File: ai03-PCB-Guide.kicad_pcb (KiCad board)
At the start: 2 copper layers, 24 parts, among them SW1 SW_Push, U1 ATmega32U4-AU, Y1 16MHz

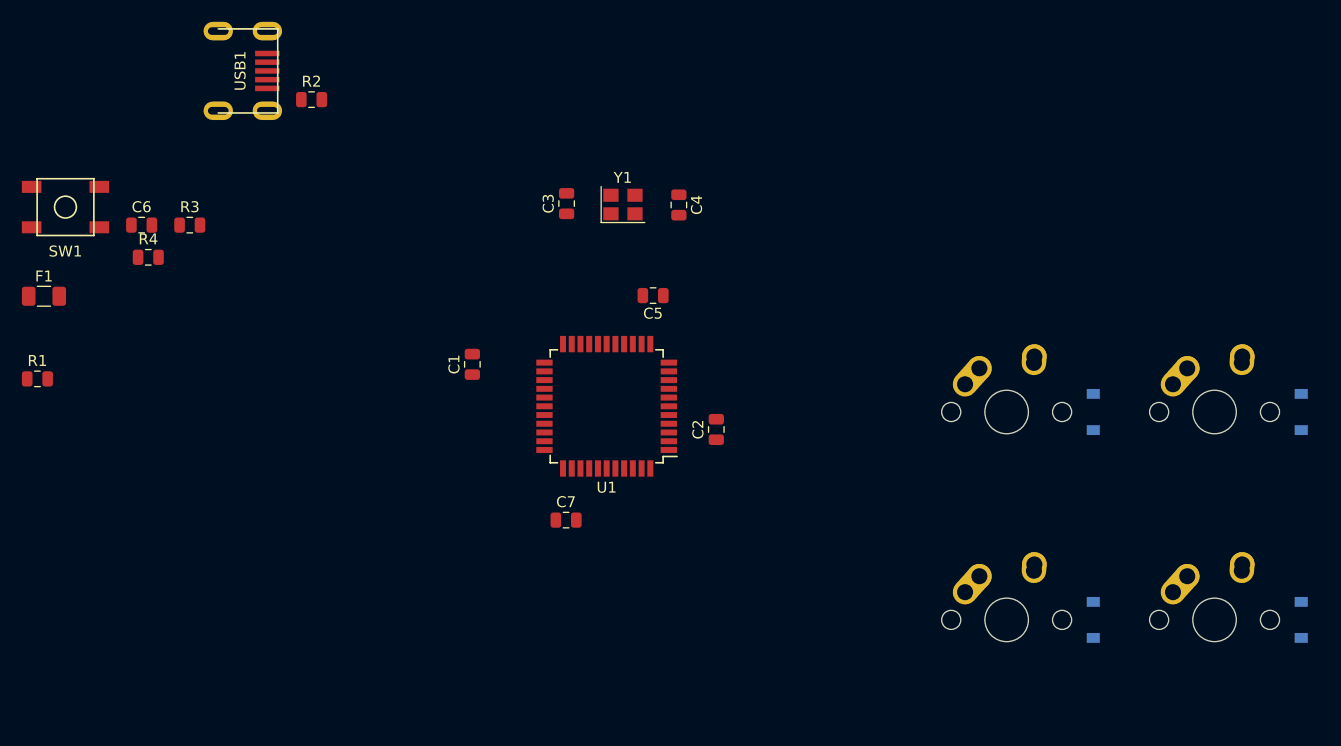
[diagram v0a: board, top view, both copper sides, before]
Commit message: Beginning Routing
This is the step just before the beginning of Routing. I've smoothed out the corners so as not to get cuts if it's printed. Setting a new Routing size called POWER for any power cables, and increasing the default size to 10mm. Now we connect everything together.
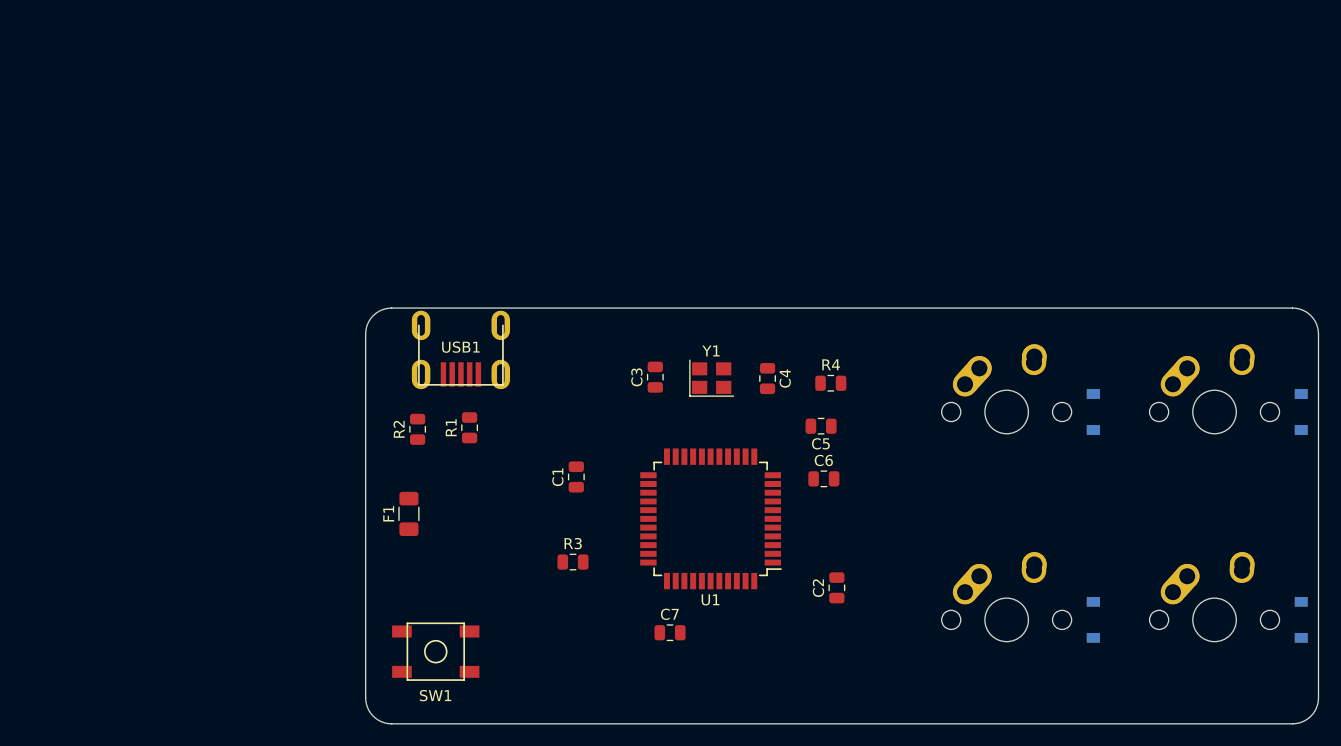
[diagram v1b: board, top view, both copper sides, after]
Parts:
- moved C6 66.7 mm to (153.1, 76.0)
- moved R4 63.6 mm to (153.7, 67.2)
- moved SW1 53.0 mm to (117.5, 91.8)
- moved R3 46.8 mm to (130.1, 83.6)
- moved R1 39.9 mm to (120.7, 71.3), turned to 90 degrees
- moved F1 38.9 mm to (115.1, 79.2), turned to 90 degrees
- moved USB1 32.2 mm to (119.9, 61.9), turned to 270 degrees
- moved R2 31.7 mm to (115.9, 71.4), turned to 90 degrees
- moved C5 19.5 mm to (152.9, 71.2)
- moved C2 18.2 mm to (154.3, 86.0)
- moved C4 17.9 mm to (148.0, 66.8)
- moved C3 17.9 mm to (137.7, 66.7)
- moved Y1 17.9 mm to (142.8, 66.7)
- moved U1 14.0 mm to (142.7, 79.6)
- moved C1 14.0 mm to (130.4, 75.8)
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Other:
- board outline added: 87.3 x 38.1 mm
- net class Default: trace_width 0.25 -> 0.254
- net class Power added: clearance 0.2, trace_width 0.381, via_dia 0.8, via_drill 0.4

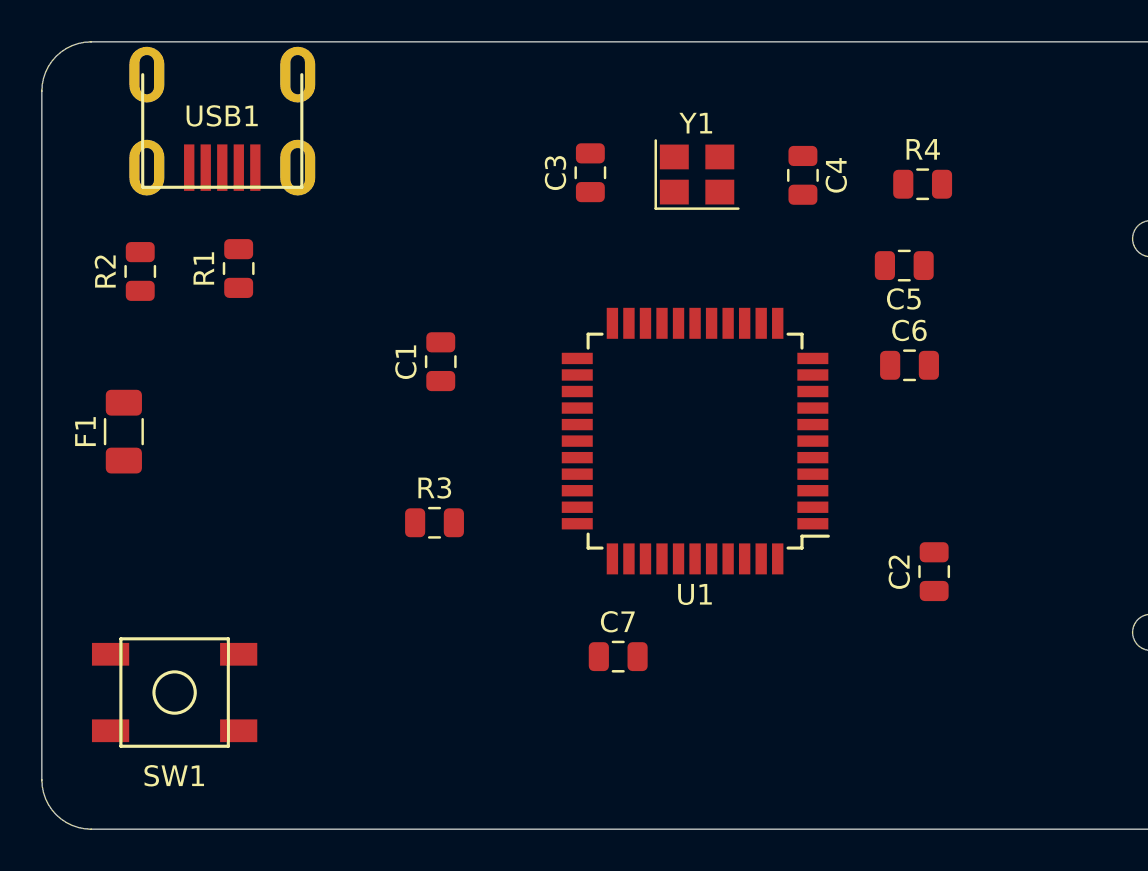
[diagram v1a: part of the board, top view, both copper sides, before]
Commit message: The bottom of the board
Hadn't put all the SMD components on the underside of the board. This is infuriating as it meant I basically had to flip and completely reorganise the layout of the SMD components.
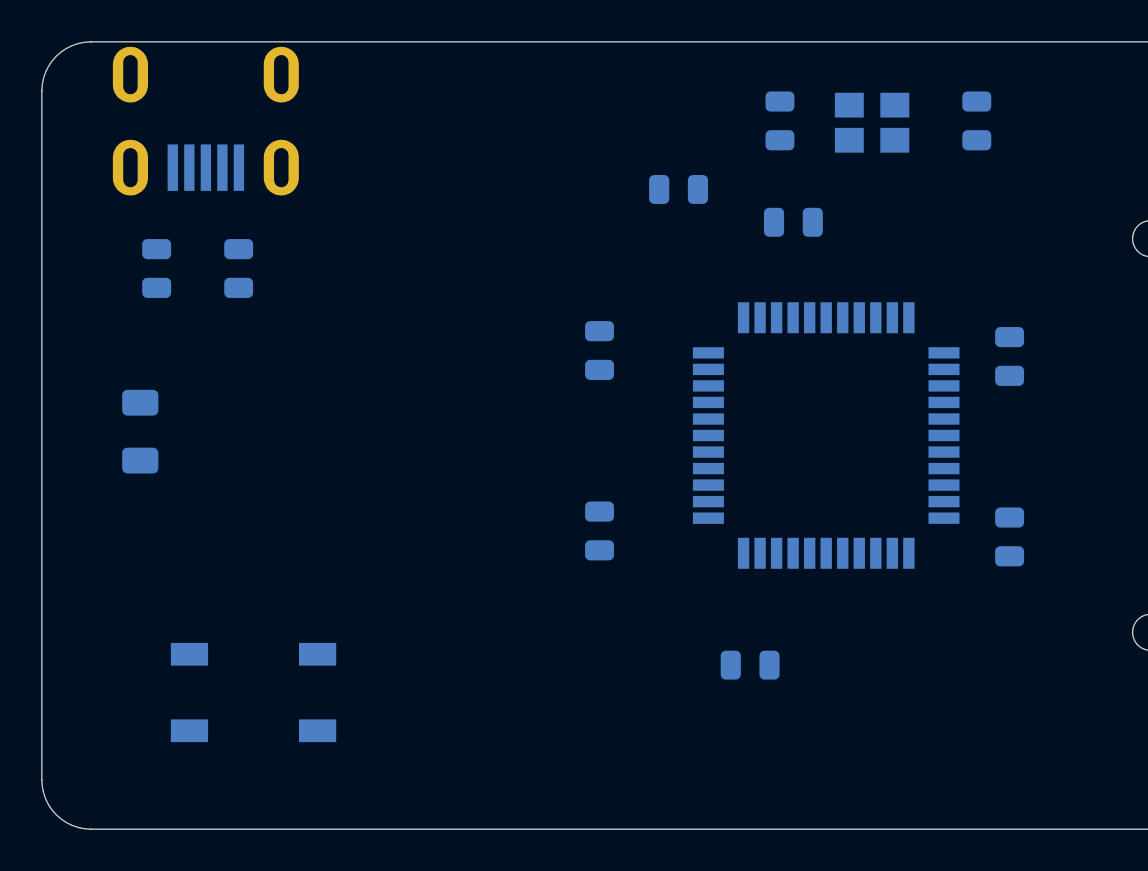
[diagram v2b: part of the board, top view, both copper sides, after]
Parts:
- C1, C2, C3, C4, C5, C6, C7, F1, R1, R2, R3, R4, SW1, U1, USB1, Y1: moved to B.Cu
- moved R3 27.8 mm to (158.0, 84.3), turned to 90 degrees
- moved C3 18.9 mm to (156.4, 64.2)
- moved C2 16.3 mm to (138.1, 84.0)
- moved C6 15.0 mm to (138.1, 75.3), turned to 270 degrees
- moved C1 14.2 mm to (141.9, 67.5), turned to 0 degrees
- moved Y1 8.83 mm to (151.3, 64.2), turned to 180 degrees
- moved C5 6.73 mm to (158.0, 75.5), turned to 90 degrees
- moved R4 6.52 mm to (147.5, 69.1), turned to 180 degrees
- moved C7 6.40 mm to (145.4, 90.5)
- moved U1 6.35 mm to (149.1, 79.4), turned to 0 degrees
- moved R2 4.76 mm to (120.7, 71.3)
- moved R1 3.97 mm to (116.7, 71.3)
- moved SW1 3.82 mm to (121.4, 91.8), turned to 180 degrees
- moved C4 2.86 mm to (146.8, 64.2)
- moved F1 0.79 mm to (115.9, 79.2)
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
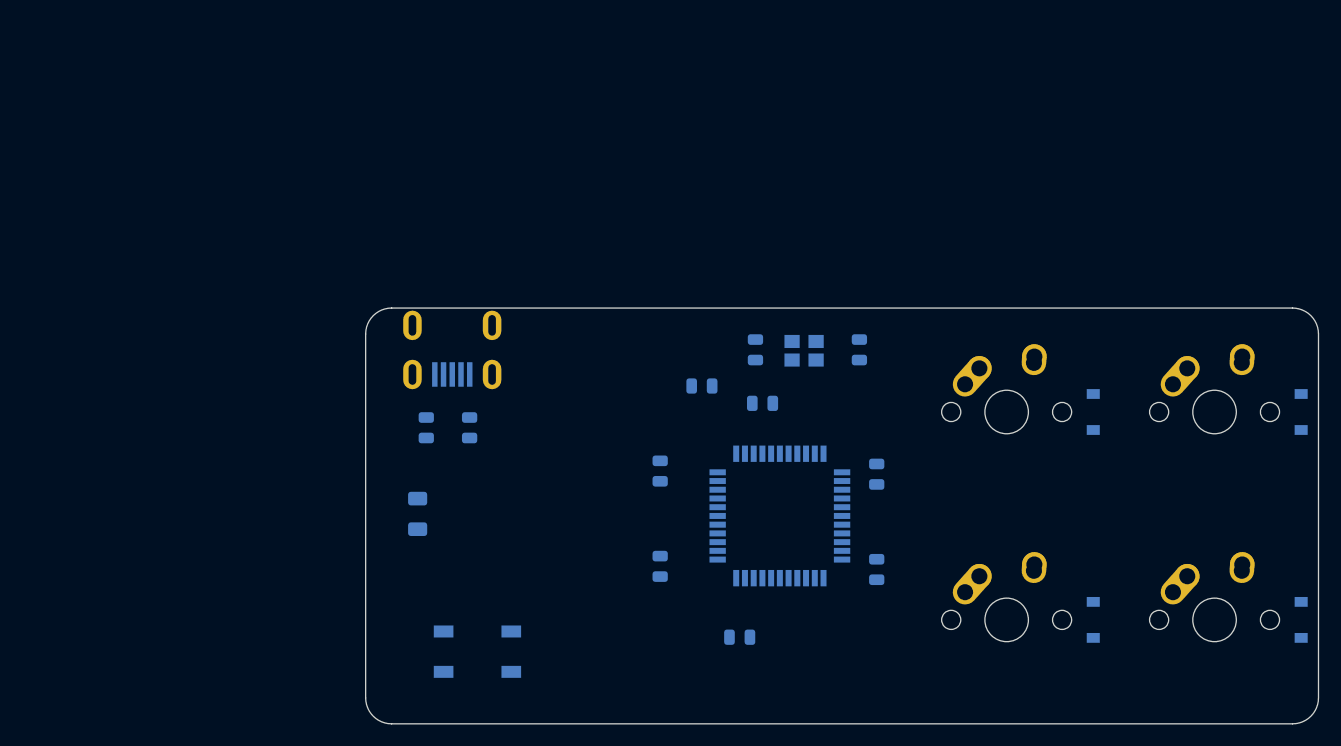
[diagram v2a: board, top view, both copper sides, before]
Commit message: PCB Finished
It's a bit messy because of the way that I had wired everything in the schematic. and due to laziness I couldn't be bothered to change it. BUt what we have here is a finalised PCB and Schematic that in theory should work when Routed and souldered.
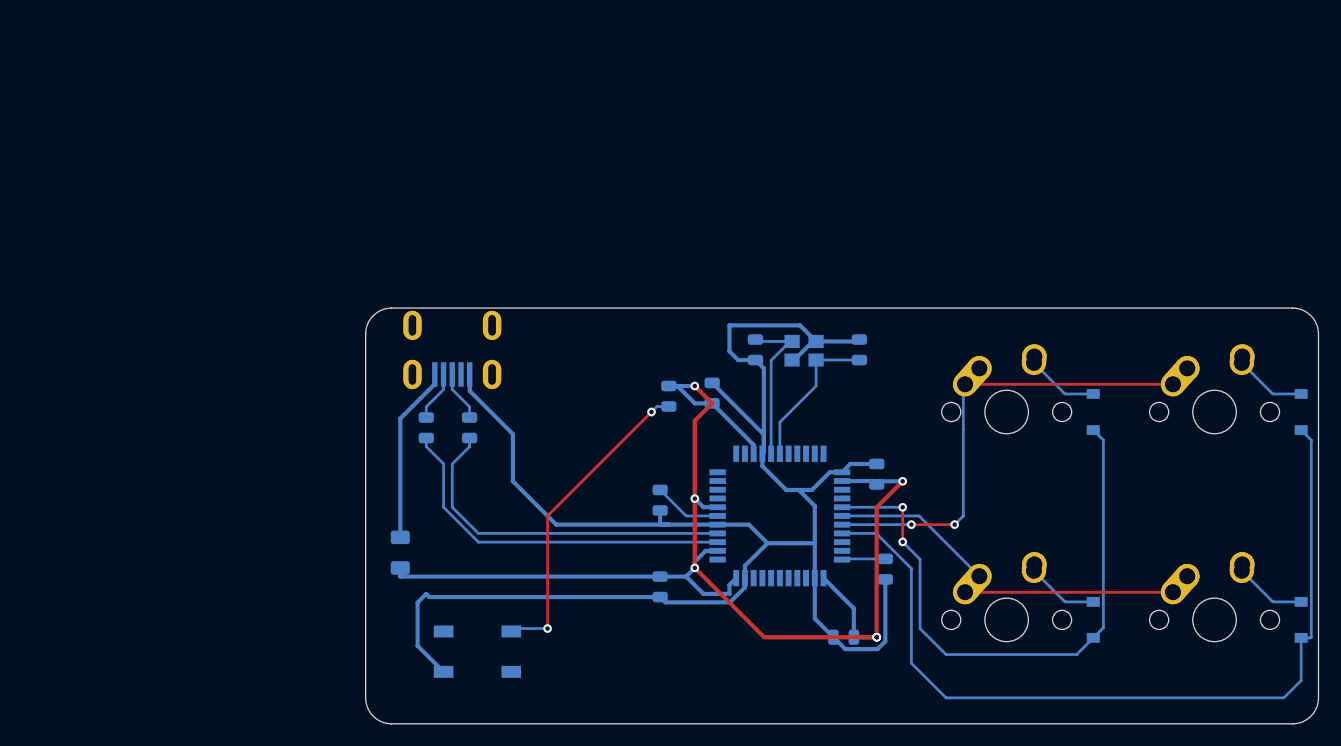
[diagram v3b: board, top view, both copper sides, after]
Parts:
- moved C7 9.53 mm to (154.9, 90.5), turned to 180 degrees
- moved R4 8.61 mm to (138.9, 68.4), turned to 270 degrees
- moved F1 3.89 mm to (114.3, 82.7), turned to 270 degrees
- moved C6 2.67 mm to (138.1, 77.9)
- moved C2 1.88 mm to (138.1, 85.9), turned to 270 degrees
- moved C1 1.14 mm to (142.9, 68.1), turned to 90 degrees
- moved R3 0.79 mm to (158.8, 84.2)
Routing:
- net GND: track 0.00 -> 163.8 mm
- net +5V: track 0.00 -> 120.6 mm, vias 0 -> 6
- net ROW1: track 0.00 -> 78.3 mm
- net ROW0: track 0.00 -> 54.6 mm, vias 0 -> 2
- net COL0: track 0.00 -> 42.4 mm, vias 0 -> 2
- net COL1: track 0.00 -> 33.9 mm
- net Net-(R1-Pad1): track 0.00 -> 33.4 mm
- net Net-(R2-Pad1): track 0.00 -> 32.3 mm
- net Net-(R4-Pad2): track 0.00 -> 29.0 mm, vias 0 -> 2
- net VCC: track 0.00 -> 16.2 mm
- net Net-(C4-Pad1): track 0.00 -> 14.6 mm
- net Net-(C3-Pad1): track 0.00 -> 13.9 mm
- net Net-(D2-Pad2): track 0.00 -> 6.62 mm
- net Net-(D1-Pad2): track 0.00 -> 6.62 mm
- net Net-(D4-Pad2): track 0.00 -> 6.62 mm
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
